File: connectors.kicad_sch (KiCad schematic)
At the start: 4 parts

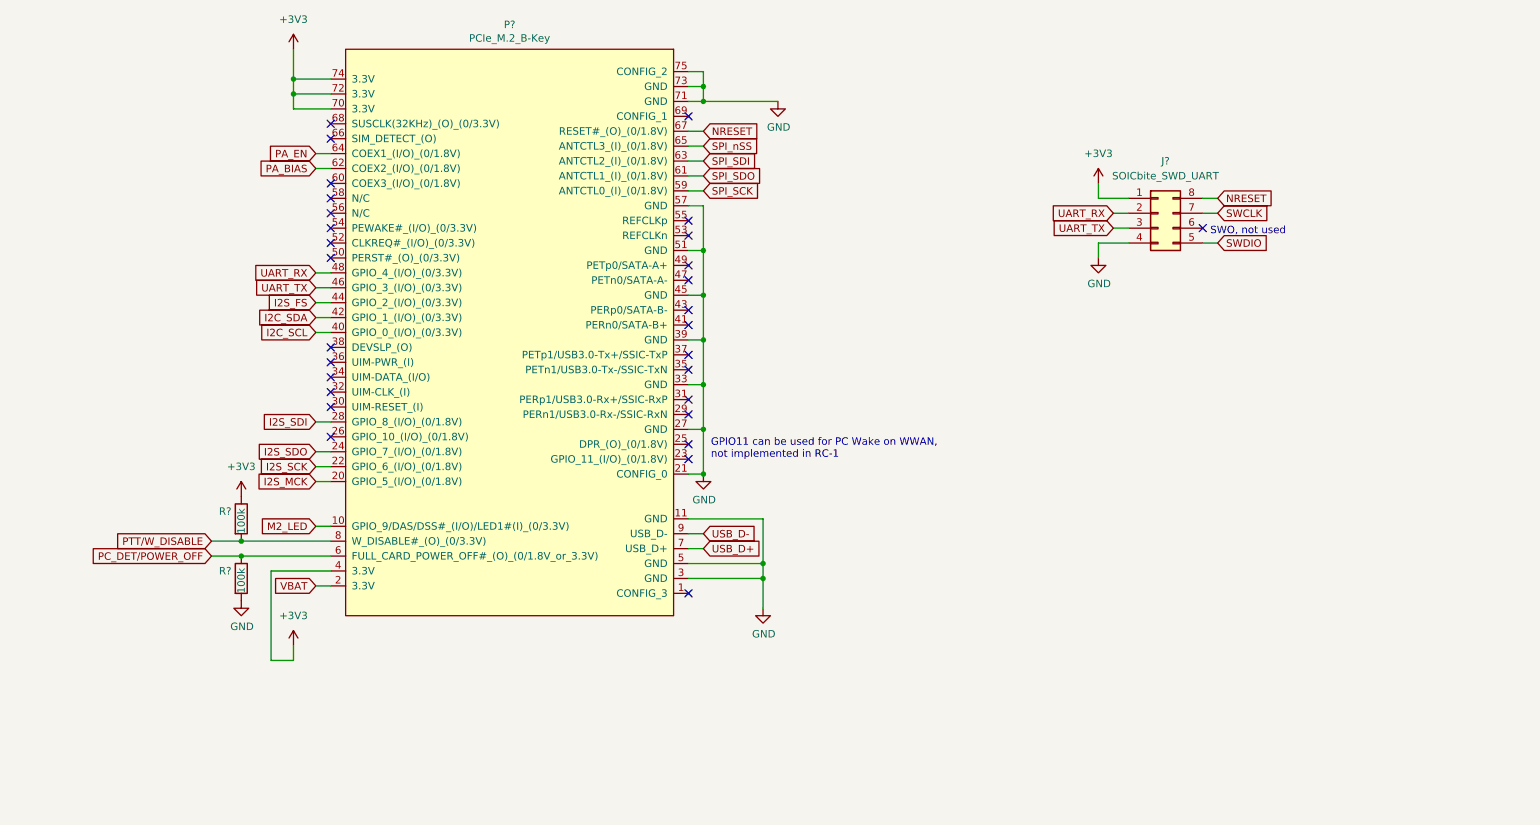
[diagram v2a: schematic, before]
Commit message: Schematic revision, details below.
[M.2 connector]
- Disconnected NRESET signal from pin 67 (RESET#_(O)_(O/1.8V)) as this would have caused a dangerous back-feed of 3.3V in a signal specified for 1.8V
- Moved I2S_FS signal to pin 26 to group it together the other I2S lines.
- Moved USART signals to pins 40 and 42.
- Moved I2C signals to pins 44 and 46.
- Replaced VBAT global label with '+BATT' power symbol.

[MCU]
- Replaced VBAT global label with '+BATT' global symbol.
- Added two more 100nF bypass capacitors for VDDIO pins.
- Removed wrong connection of VDDCORE to 3V3 power net.
- Connected 8MHz crystal directly to the corresponding pins, removed the global labels.
- Connected the 32kHz crystal directly to the corresponding pins, removed the global labels and changed its value to 32.768kHz.
- Changed the value of crystal load capacitors to 'TBD', as their value depends both on the chosen crystal and on PCB layout.
- Added notes for PCB routing.
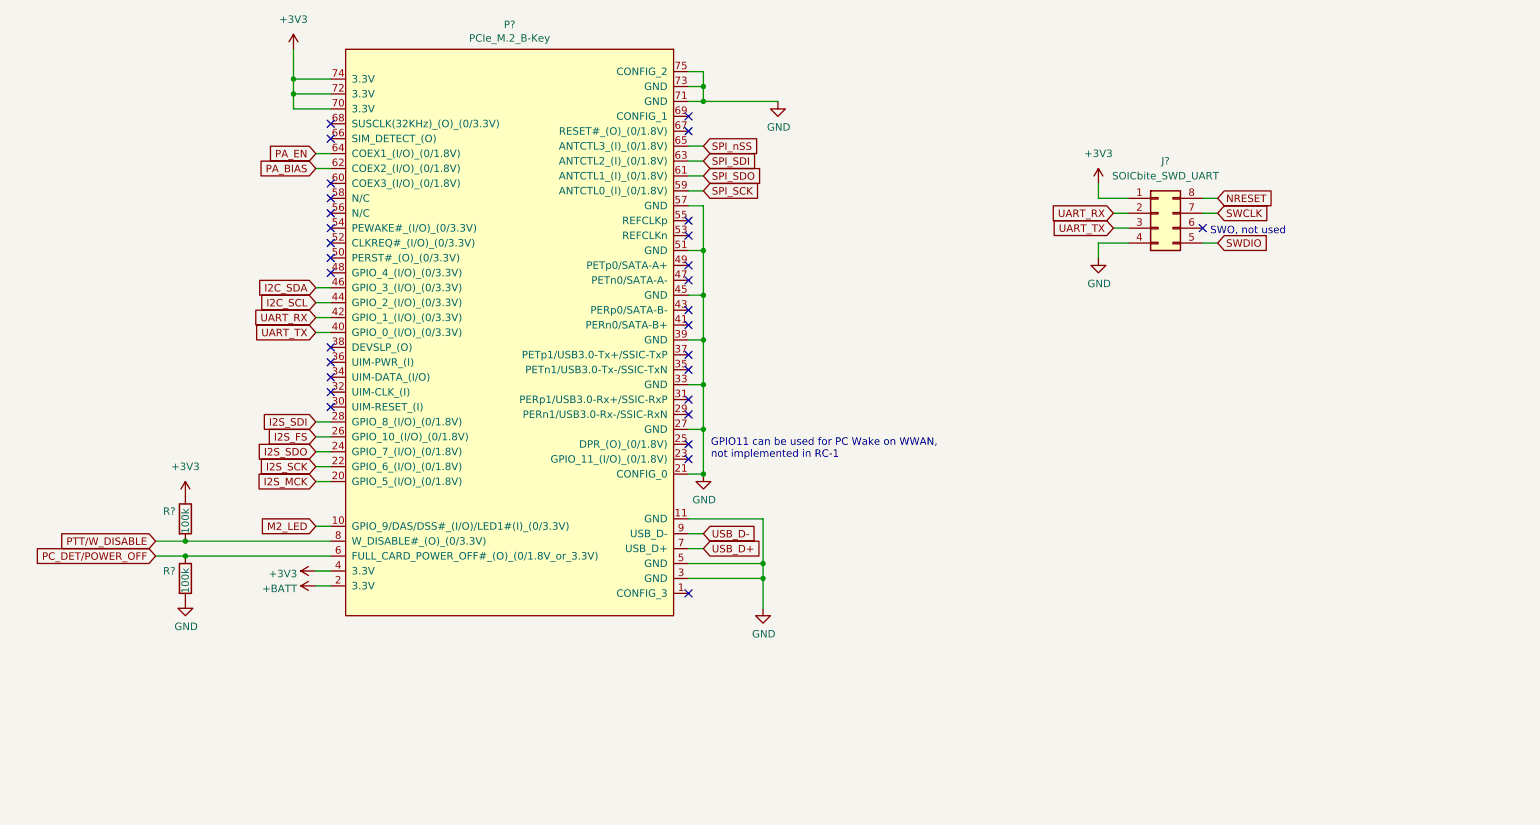
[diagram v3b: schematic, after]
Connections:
- net I2C_SCL: now also P?.44 (GPIO_2_(I/O)_(0/3.3V)); no longer P?.40 (GPIO_0_(I/O)_(0/3.3V))
- net I2C_SDA: now also P?.46 (GPIO_3_(I/O)_(0/3.3V)); no longer P?.42 (GPIO_1_(I/O)_(0/3.3V))
- net I2S_FS: now also P?.26 (GPIO_10_(I/O)_(0/1.8V)); no longer P?.44 (GPIO_2_(I/O)_(0/3.3V))
- net NRESET: no longer P?.67 (RESET#_(O)_(0/1.8V))
- net UART_RX: now also P?.42 (GPIO_1_(I/O)_(0/3.3V)); no longer P?.48 (GPIO_4_(I/O)_(0/3.3V))
- net UART_TX: now also P?.40 (GPIO_0_(I/O)_(0/3.3V)); no longer P?.46 (GPIO_3_(I/O)_(0/3.3V))
- net VBAT renamed +BATT
- no-connect marks 29 -> 30
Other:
- moved on the sheet: R?

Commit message: Added interfacing transistors for LED and nRESET signals on M.2 connector, switched from global to hierarchical net labels
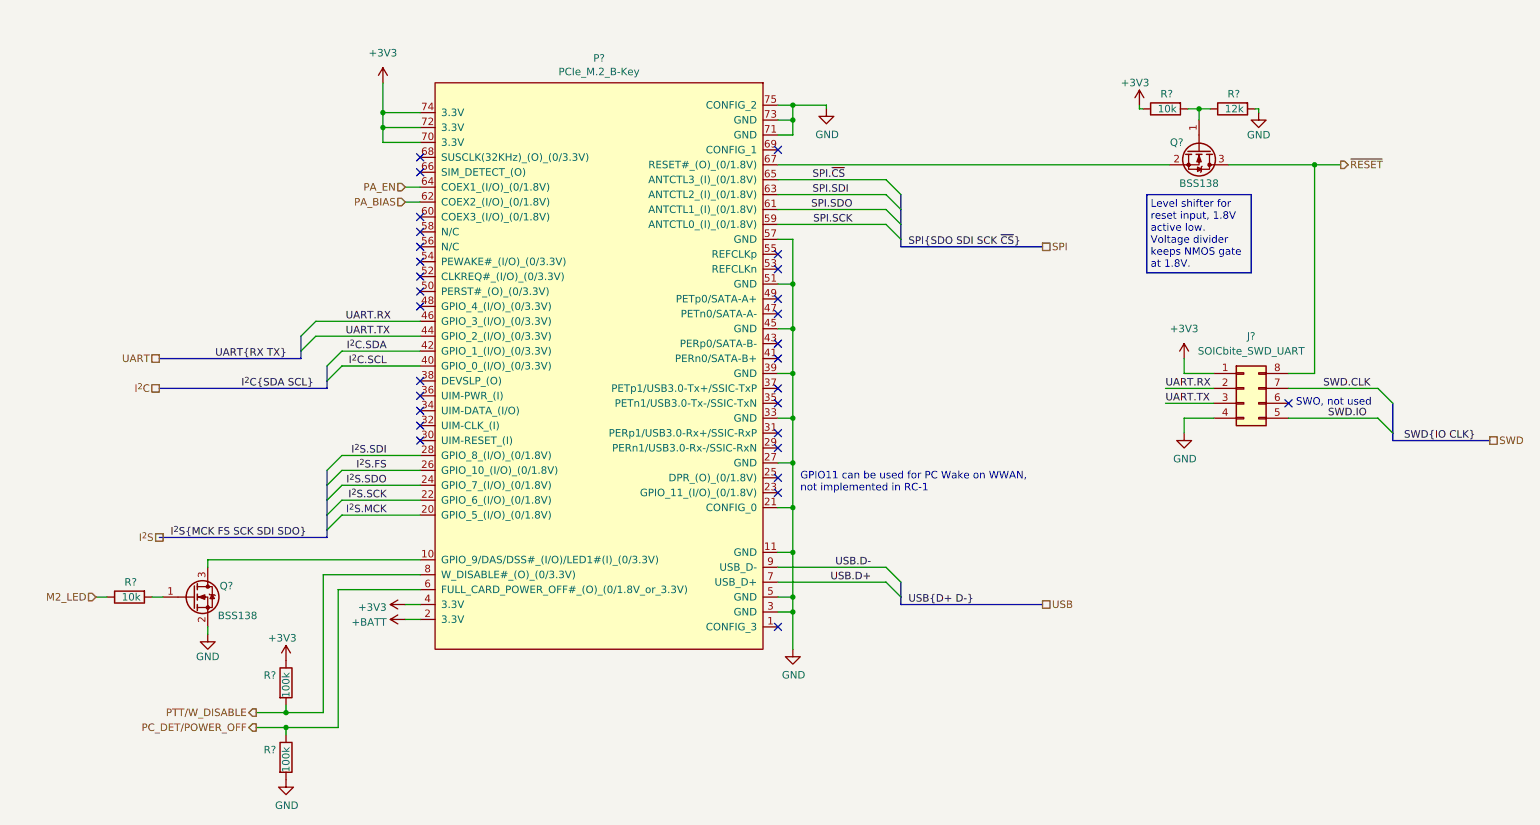
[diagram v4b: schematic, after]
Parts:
- added Q? (x2): BSS138, Package_TO_SOT_SMD:SOT-23, symbol Transistor_FET:BSS138
- added R? (x2): 10k, Resistor_SMD:R_0402_1005Metric, symbol Device:R
- added R?: 12k, Resistor_SMD:R_0402_1005Metric, symbol Device:R
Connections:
- net +3V3: now also R?.1
- net GND: now also Q?.2 (S), R?.2
- net M2_LED: now also R?.1; no longer P?.10 (GPIO_9/DAS/DSS#_(I/O)/LED1#(I)_(0/3.3V))
- net at P?.67 (RESET#_(O)_(0/1.8V)): now also Q?.2 (S)
- net I2C_SCL renamed UART.TX
- net UART.TX: now also J?.3 (Pin_3)
- net I2C_SDA renamed UART.RX
- net UART.RX: now also J?.2 (Pin_2)
- net I2S_FS renamed I^{2}S.FS
- net I2S_MCK renamed I^{2}S.MCK
- net I2S_SCK renamed I^{2}S.SCK
- net I2S_SDI renamed I^{2}S.SDI
- net I2S_SDO renamed I^{2}S.SDO
- net NRESET renamed ~{RESET}
- net ~{RESET}: now also Q?.3 (D)
- net SPI_SCK renamed SPI.SCK
- net SPI_SDI renamed SPI.SDI
- net SPI_SDO renamed SPI.SDO
- net SPI_nSS renamed SPI.~{CS}
- net SWCLK renamed SWD.CLK
- net SWDIO renamed SWD.IO
- net UART_RX renamed I^{2}C.SDA
- net I^{2}C.SDA: no longer J?.2 (Pin_2)
- net UART_TX renamed I^{2}C.SCL
- net I^{2}C.SCL: no longer J?.3 (Pin_3)
- net USB_D+ renamed USB.D+
- net USB_D- renamed USB.D-
- new net: Q?.1 (G), R?.2
- new net: P?.10 (GPIO_9/DAS/DSS#_(I/O)/LED1#(I)_(0/3.3V)), Q?.3 (D)
- new net: Q?.1 (G), R?.1, R?.2
- no-connect marks 30 -> 29
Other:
- note added: "Level shifter for reset input, 1.8V active low. Voltage divider keeps NMOS gate at 1.8V."
- company: (none) -> OpenRTX & M17
- title: (none) -> Connectors
- moved on the sheet: J?, P?, R?
